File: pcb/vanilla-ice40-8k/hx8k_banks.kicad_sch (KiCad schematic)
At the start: 1 part, among them U1 ICE40HX8K-CT256

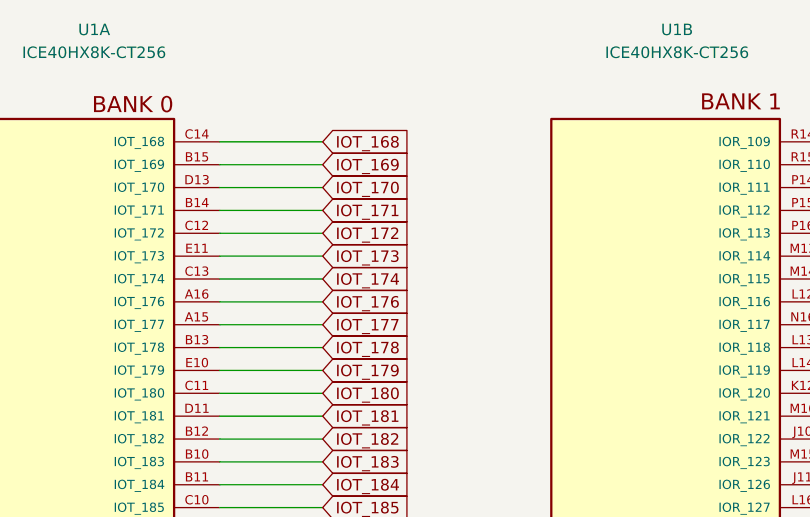
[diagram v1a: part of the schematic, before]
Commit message: [hx8k][pcb] route usb data
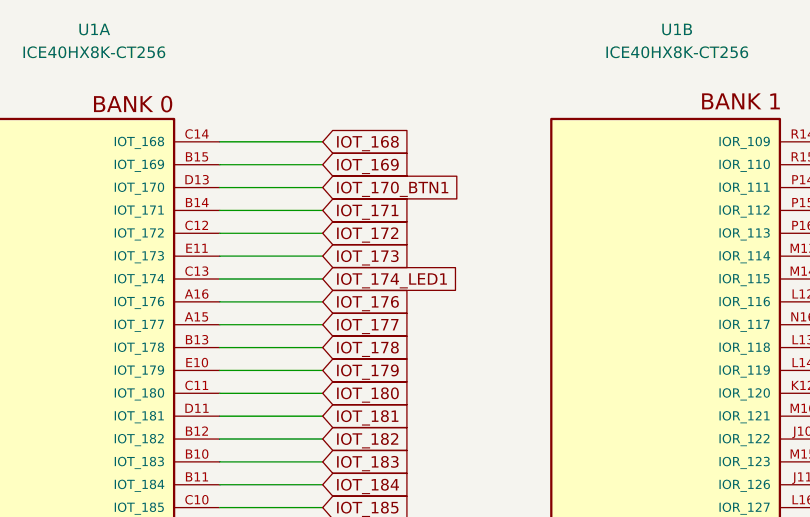
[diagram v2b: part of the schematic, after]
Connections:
- net IOT_170 renamed IOT_170_BTN1
- net IOT_174 renamed IOT_174_LED1
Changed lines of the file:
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@@
 		)
 	)
-	(global_label "IOT_174"
+	(global_label "IOT_174_LED1"
 		(shape input)
 		(at 62.23 44.45 0)
@@
 		)
 		(property "Intersheetrefs" "${INTERSHEET_REFS}"
-			(at 72.7142 44.45 0)
+			(at 78.3384 44.45 0)
 			(effects
 				(font
@@
 		)
 	)
-	(global_label "IOT_170"
+	(global_label "IOT_170_BTN1"
 		(shape input)
 		(at 62.23 34.29 0)
@@
 		)
 		(property "Intersheetrefs" "${INTERSHEET_REFS}"
-			(at 72.7142 34.29 0)
-			(effects
-				(font
+			(at 78.4594 34.29 0)
+			(effects
+				(font

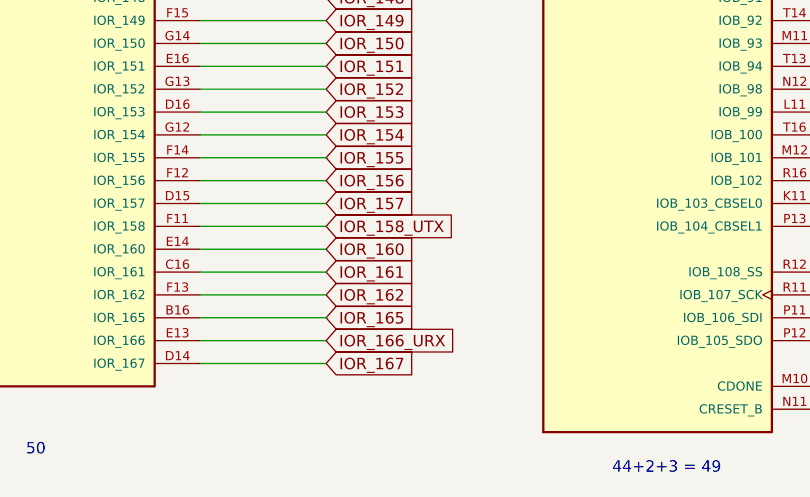
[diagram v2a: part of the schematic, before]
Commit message: [hx8k][pcb] ft routed
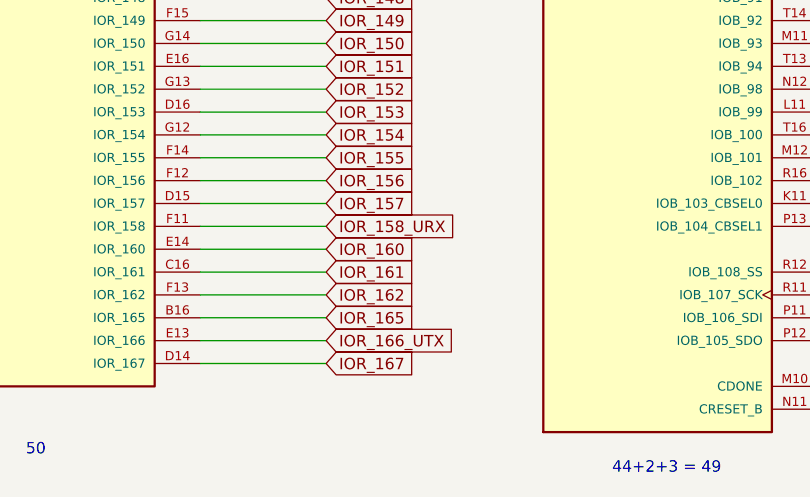
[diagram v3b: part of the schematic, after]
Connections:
- net IOR_158_UTX renamed IOR_158_URX
- net IOR_166_URX renamed IOR_166_UTX
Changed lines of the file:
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@@
 		)
 	)
-	(global_label "IOR_166_URX"
+	(global_label "IOR_166_UTX"
 		(shape input)
 		(at 132.08 156.21 0)
@@
 		)
 		(property "Intersheetrefs" "${INTERSHEET_REFS}"
-			(at 147.6442 156.21 0)
+			(at 147.3418 156.21 0)
 			(effects
 				(font
@@
 		)
 	)
-	(global_label "IOR_158_UTX"
+	(global_label "IOR_158_URX"
 		(shape input)
 		(at 132.08 143.51 0)
@@
 		)
 		(property "Intersheetrefs" "${INTERSHEET_REFS}"
-			(at 147.3418 143.51 0)
-			(effects
-				(font
+			(at 147.6442 143.51 0)
+			(effects
+				(font

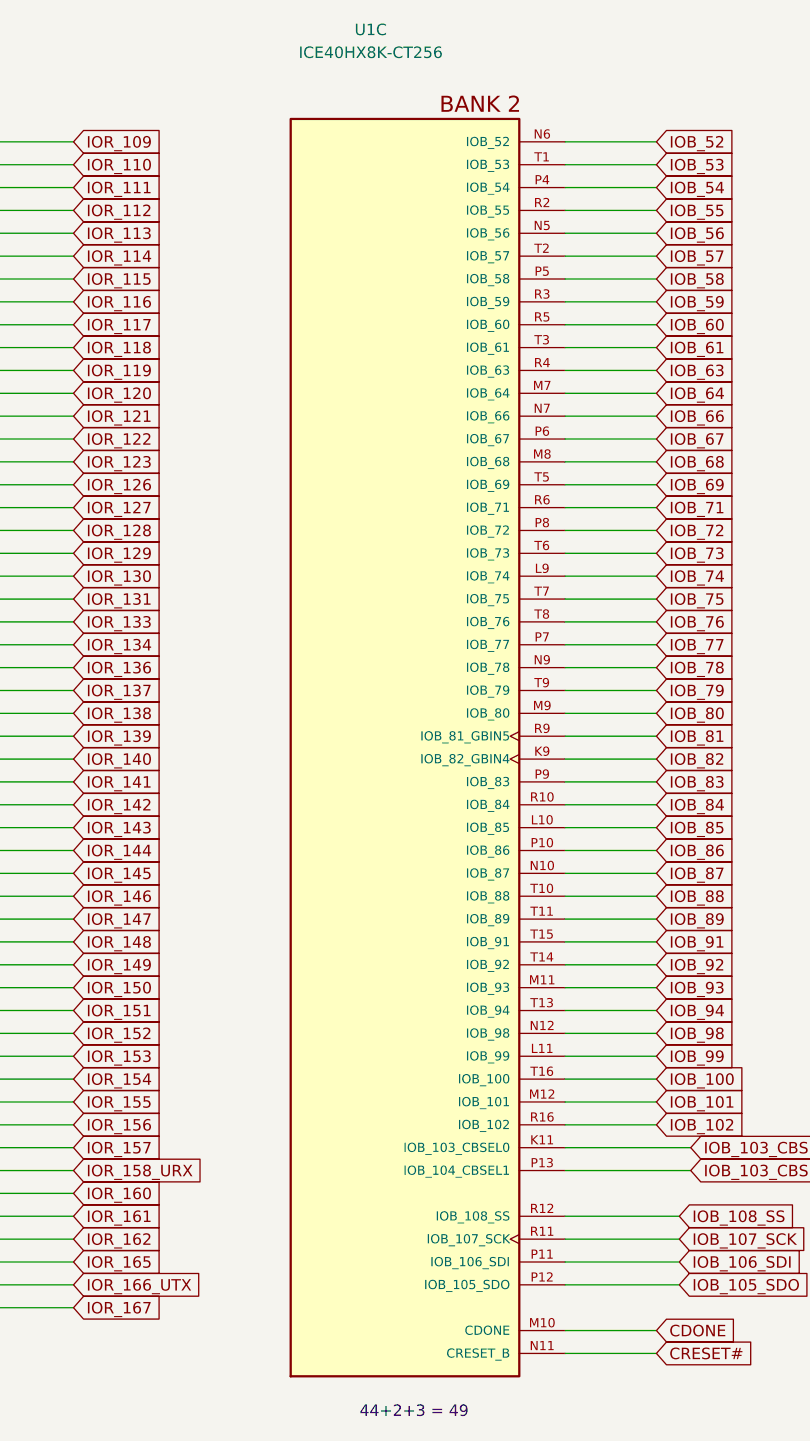
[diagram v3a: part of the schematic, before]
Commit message: [hx8k][pcb] convert all components to custom lib
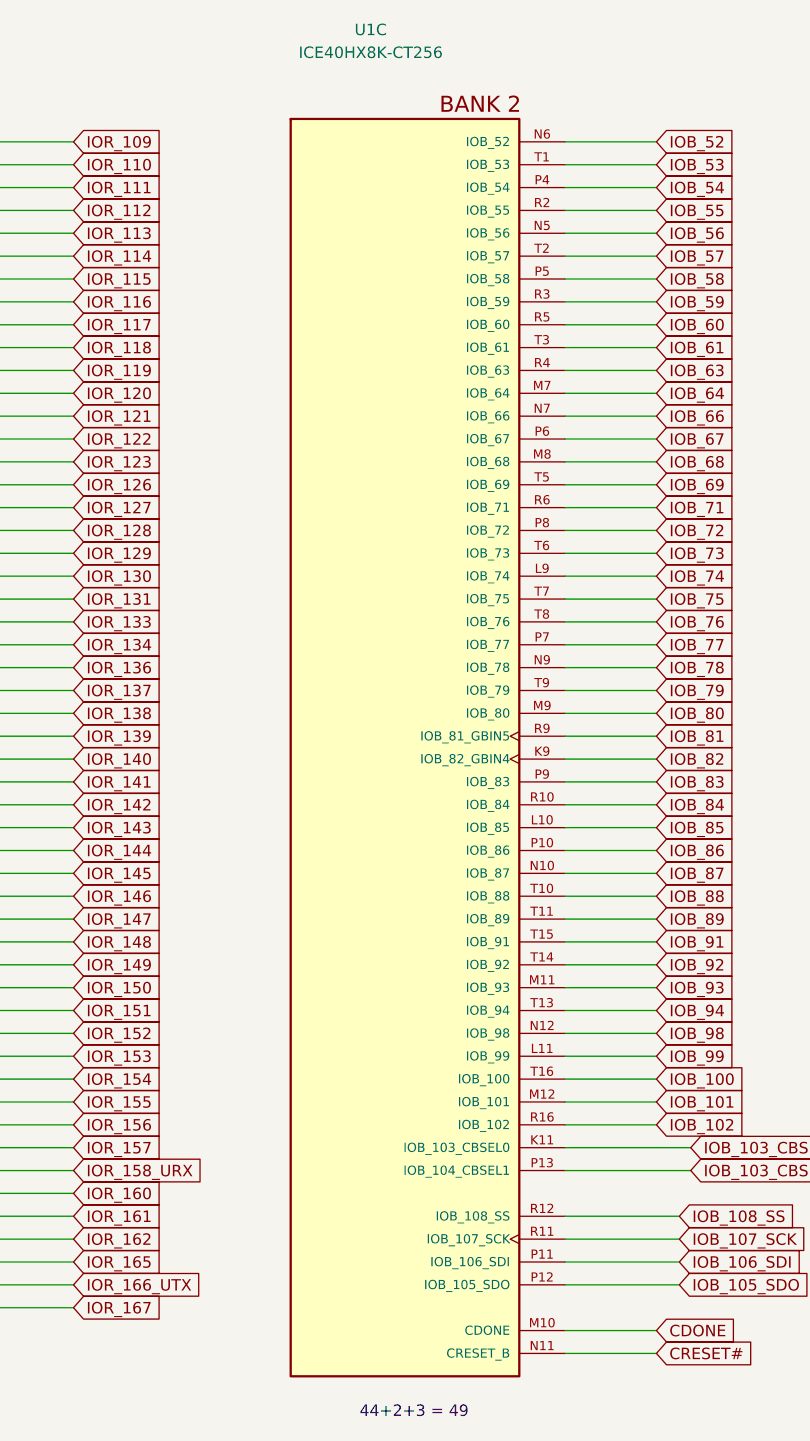
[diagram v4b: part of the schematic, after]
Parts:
- U1: footprint ICE40HX8K-CT256:BGA256C80P16X16_1400X1400X170 -> !Misc:BGA256C80P16X16_1400X1400X170; symbol ICE40HX8K-CT256:ICE40HX8K-CT256 -> !Misc:ICE40HX8K-CT256; Availability In Stock -> (none); Check_prices https://www.snapeda.com/parts/ICE40HX8K-CT256/Lattice+Semic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 -> (none); Description_1 iCE40™ HX Field Programmable Gate Array (FPGA) IC 206 13107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 -> (none); MANUFACTURER Lattice Semiconductor -> (none); MF Lattice Semiconductor -> (none); MP ICE40HX8K-CT256 -> (none); PART_REV 3.4 -> (none); Package CABGA-256 Lattice Semiconductor -> (none); Price None -> (none); STANDARD IPC-7351B -> (none); SnapEDA_Link https://www.snapeda.com/parts/ICE40HX8K-CT256/Lattice+Semic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 -> (none)

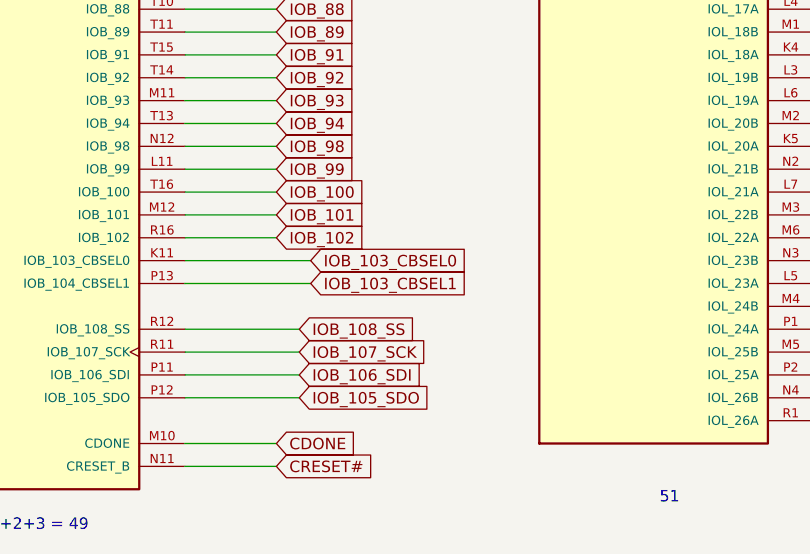
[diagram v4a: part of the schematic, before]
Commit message: [pcb][hx8k] add remaining helper labels
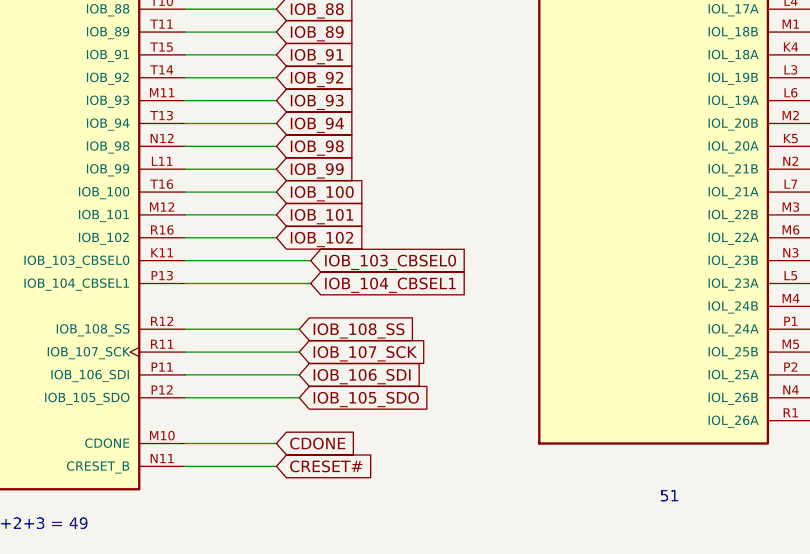
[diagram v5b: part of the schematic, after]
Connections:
- net IOB_103_CBSEL1 renamed IOB_104_CBSEL1
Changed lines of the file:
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@@
 		)
 	)
-	(global_label "IOB_103_CBSEL1"
+	(global_label "IOB_104_CBSEL1"
 		(shape input)
 		(at 200.66 143.51 0)
